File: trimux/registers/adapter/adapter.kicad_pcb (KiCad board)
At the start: 2 copper layers, 100 x 100 mm, 20 parts, among them P1 CONN_02X05, P10 CONN_02X05, P11 CONN_02X05, P12 CONN_02X05, P13 CONN_02X05, P2 CONN_02X05, P21 CONN_02X08, P22 CONN_02X08, P23 CONN_02X08, P24 CONN_02X08, P25 CONN_02X08, P26 CONN_02X08, P27 CONN_02X08, P3 CONN_02X05, P4 CONN_02X05, P5 CONN_02X05, P6 CONN_02X05, P7 CONN_02X05, P8 CONN_02X05, P9 CONN_02X05

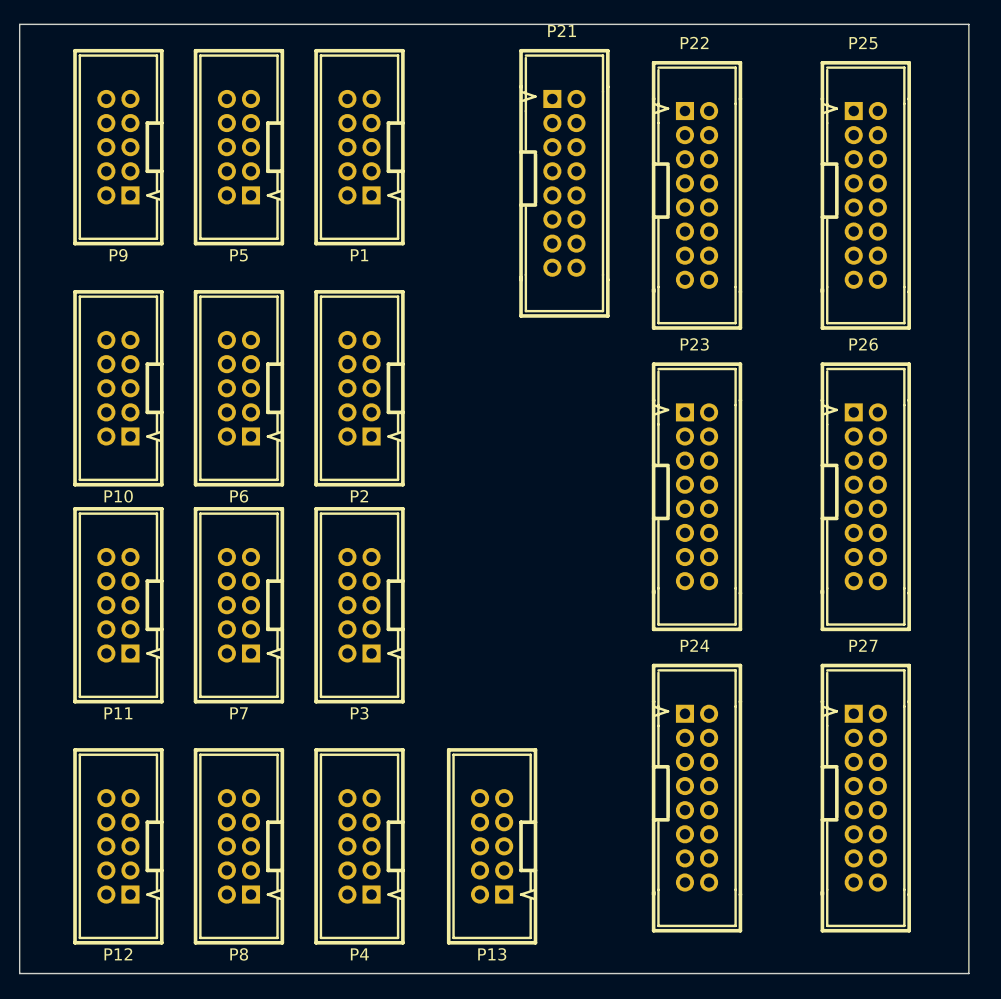
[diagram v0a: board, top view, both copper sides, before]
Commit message: 1st routing of the memory adapter board
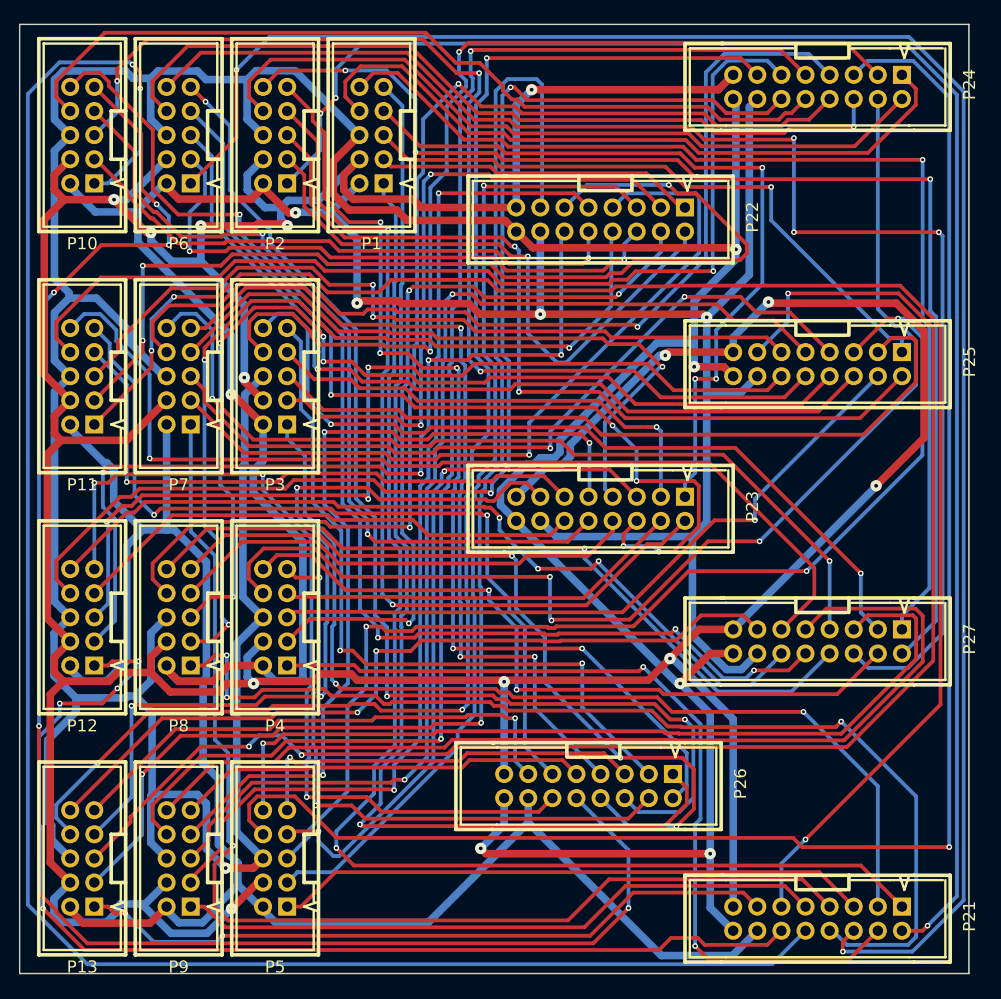
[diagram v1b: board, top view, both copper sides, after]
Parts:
- moved P21 81.9 mm to (99.1, 109.2), turned to 270 degrees
- moved P24 76.0 mm to (99.1, 21.6), turned to 270 degrees
- moved P9 75.2 mm to (31.8, 102.9)
- moved P5 75.0 mm to (41.9, 102.9)
- moved P13 43.2 mm to (21.6, 102.9)
- moved P26 42.2 mm to (74.9, 95.2), turned to 270 degrees
- moved P2 28.1 mm to (41.9, 26.7)
- moved P6 27.4 mm to (31.8, 26.7)
- moved P10 26.9 mm to (21.6, 26.7)
- moved P3 25.7 mm to (41.9, 52.1)
- moved P4 25.7 mm to (41.9, 77.5)
- moved P7 25.0 mm to (31.8, 52.1)
- moved P8 25.0 mm to (31.8, 77.5)
- moved P11 24.4 mm to (21.6, 52.1)
- moved P12 24.4 mm to (21.6, 77.5)
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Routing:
- net /GND: track 0.00 -> 483.1 mm, vias 0 -> 13
- net /-5V: track 0.00 -> 471.3 mm, vias 0 -> 6
- net /+5V: track 0.00 -> 448.9 mm, vias 0 -> 5
- net /C10: track 0.00 -> 199.6 mm, vias 0 -> 2
- net /C6: track 0.00 -> 197.2 mm, vias 0 -> 2
- net /Qm10: track 0.00 -> 177.8 mm, vias 0 -> 5
- net /C2: track 0.00 -> 174.7 mm, vias 0 -> 3
- net /Al5: track 0.00 -> 171.4 mm, vias 0 -> 1
- net /C11: track 0.00 -> 170.6 mm, vias 0 -> 3
- net /Qh13: track 0.00 -> 158.6 mm, vias 0 -> 3
- net /Al13: track 0.00 -> 151.4 mm, vias 0 -> 3
- net /Ql6: track 0.00 -> 150.5 mm, vias 0 -> 3
- net /Al9: track 0.00 -> 147.6 mm, vias 0 -> 2
- net /Ah13: track 0.00 -> 138.0 mm, vias 0 -> 2
- net /C1: track 0.00 -> 136.3 mm, vias 0 -> 1
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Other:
- net class Default: trace_width 0.5 -> 0.4; via_dia 0.8 -> 0.6; via_drill 0.4 -> 0.3

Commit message: adapter board final routing
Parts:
- added REF**: 1pin, Connectors:1pin, F.Cu at (110.0, 95.6)
- added REF**: 1pin, Connectors:1pin, F.Cu at (70.1, 18.4)
- added REF**: 1pin, Connectors:1pin, F.Cu at (21.7, 90.2)
- moved P23 8.51 mm to (83.8, 69.9)
- moved P22 5.08 mm to (81.1, 37.0)
- moved P1 4.95 mm to (57.0, 26.6)
- moved P25 3.40 mm to (99.1, 54.2)
- moved P27 3.25 mm to (98.8, 83.3)
- moved P26 3.21 mm to (77.5, 97.2)
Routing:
- net /C6: track 197.2 -> 144.8 mm
- net /Qh13: track 158.6 -> 116.6 mm, vias 3 -> 2
- net /Ah11: track 106.2 -> 67.3 mm, vias 3 -> 2
- net /C2: track 174.7 -> 140.4 mm, vias 3 -> 2
- net /C11: track 170.6 -> 137.6 mm
- net /-5V: track 471.3 -> 501.9 mm, vias 6 -> 4
- net /Ql7: track 93.2 -> 123.4 mm, vias 2 -> 1
- net /Qm1: track 120.6 -> 91.6 mm, vias 1 -> 0
- net /Qm10: track 177.8 -> 149.0 mm, vias 5 -> 0
- net /Al9: track 147.6 -> 174.7 mm
- net /Qh10: track 117.6 -> 92.8 mm, vias 3 -> 2
- net /GND: track 483.1 -> 459.5 mm, vias 13 -> 7
- net /Ah13: track 138.0 -> 114.4 mm
- net /+5V: track 448.9 -> 469.5 mm, vias 5 -> 6
- net /Qm11: track 88.1 -> 102.4 mm, vias 2 -> 1
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
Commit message: memory
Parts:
- added C1: 104, Capacitors_SMD:C_1206_HandSoldering, B.Cu at (68.7, 105.0)
- added C2: 104, Capacitors_SMD:C_1206_HandSoldering, B.Cu at (66.5, 102.2)
- added C3: 47u, Capacitors_THT:CP_Radial_D5.0mm_P2.00mm, F.Cu at (96.6, 62.3)
- added C4: 47u, Capacitors_THT:CP_Radial_D5.0mm_P2.00mm, F.Cu at (55.8, 107.6)
- added J1: Conn_01x03, Pin_Headers:Pin_Header_Straight_1x03_Pitch2.54mm, F.Cu at (108.2, 32.8)
- moved REF** 1.70 mm to (110.7, 97.2)
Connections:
- net /+5V renamed +5V
- net /-5V renamed -5V
- net /GND renamed GNDREF
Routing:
- net GNDREF: track 459.5 -> 507.9 mm, vias 7 -> 8
- net +5V: track 469.5 -> 496.1 mm, vias 6 -> 7
- net -5V: track 501.9 -> 525.5 mm, vias 4 -> 5
- net /C3: track 110.6 -> 116.5 mm
- net /Qh4: track 76.5 -> 79.9 mm
- net /Ql2: track 127.0 -> 129.9 mm
- net /Al5: track 161.2 -> 163.1 mm
- net /Ql6: track 149.9 -> 151.7 mm
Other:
- board text added: "-5 0 +5"
- board text added: "A high"
- board text added: "A low"
- board text added: "A middle"
- board text added: "CLOCK"
- board text added: "Q high"
- board text added: "Q low"
- board text added: "Q middle"
- board text added: "Registers-to-1:13 multiplexers adapter board"
